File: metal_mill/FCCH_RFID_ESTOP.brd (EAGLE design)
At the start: 100 x 40 mm, 34 parts, among them Q1 2N3565, Q2 2N3565, Q3 2N3906, Q4 2N3906, Q5 2N3906

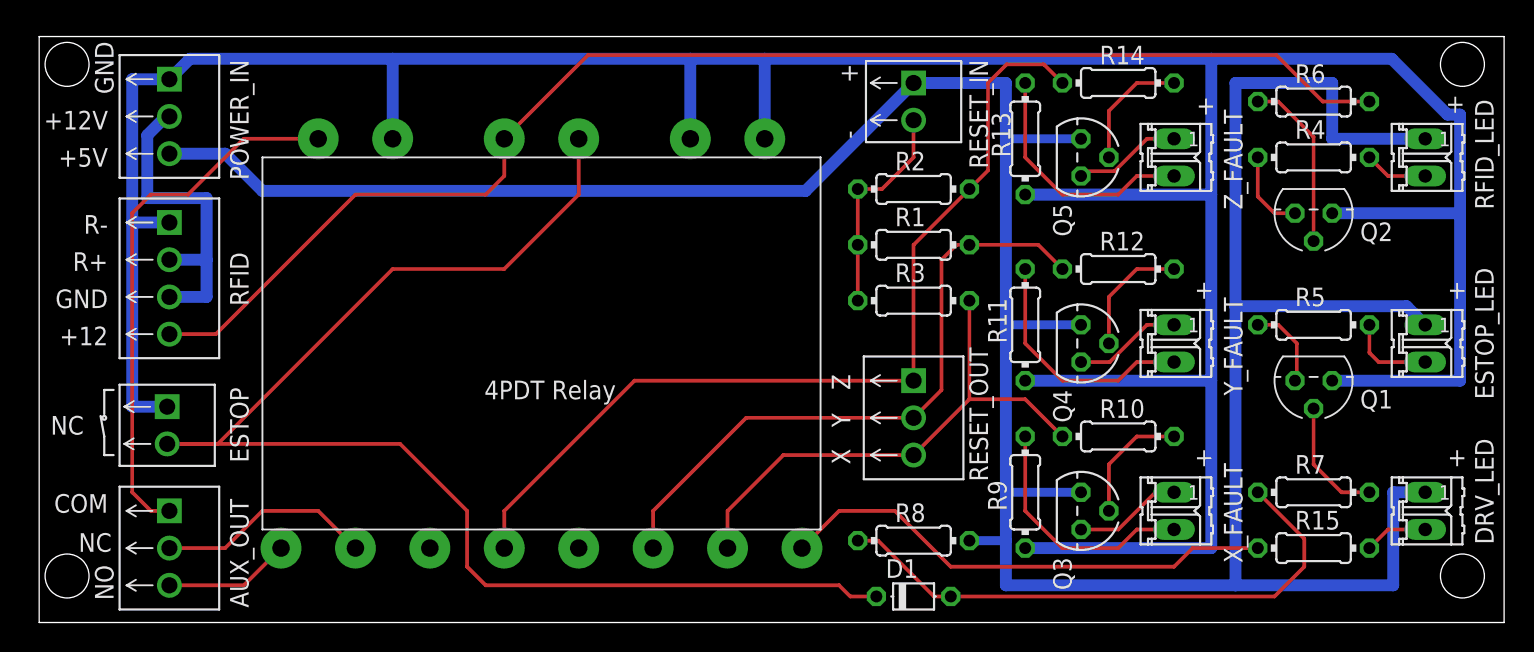
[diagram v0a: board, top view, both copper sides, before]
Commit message: check point: before changing the reset relay to allow +5V as well as ground
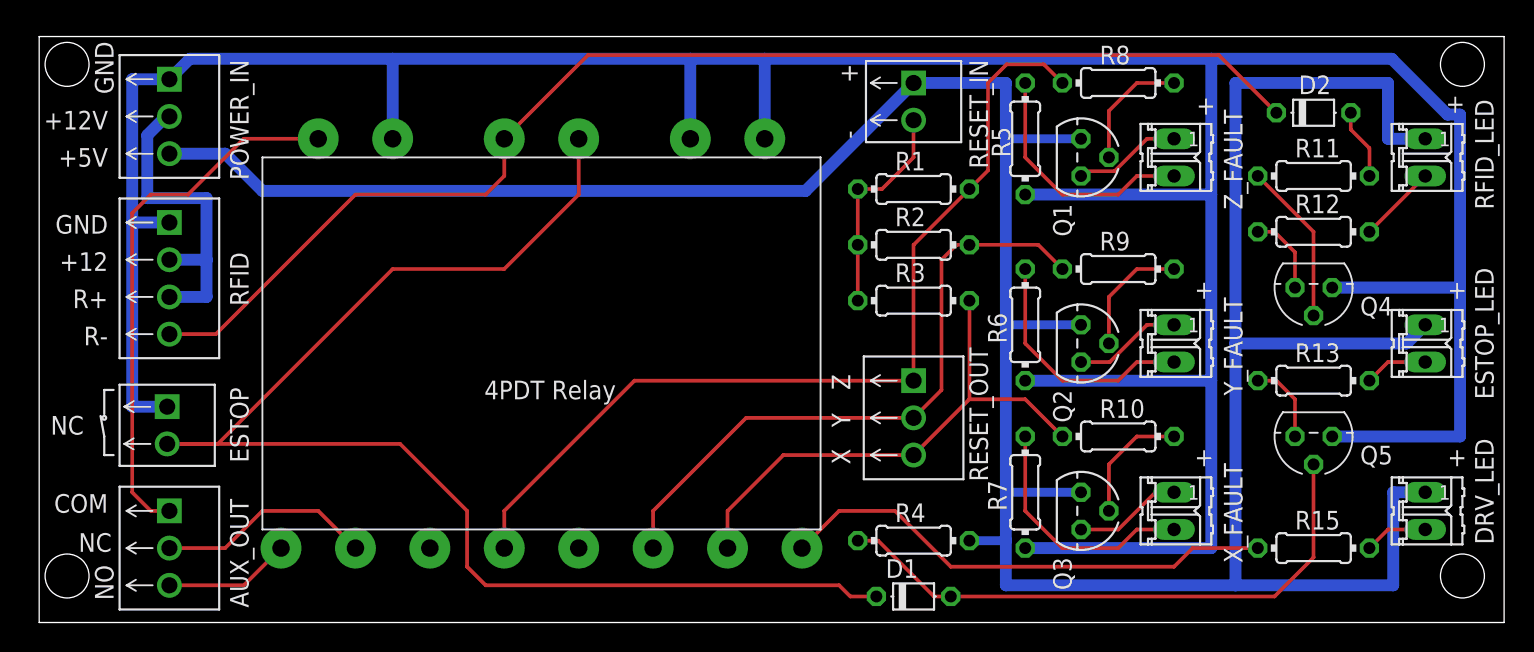
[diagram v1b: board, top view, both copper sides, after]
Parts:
- removed R14: (no value), rcl:0204/7
- added D2: (no value), diode:D-5
- Q1, Q2: value 2N3565 -> 2N3906; device transistor-npn:TO92 -> transistor-pnp:TO92
- Q4, Q5: value 2N3906 -> 2N3565; device transistor-pnp:TO92 -> transistor-npn:TO92
- R1, R2, R3: value (none) -> 4.7k
- R10, R11, R4, R8, R9: value (none) -> 2k
- R12, R13, R15, R5, R6, R7: value (none) -> 150
- moved R4 37.8 mm to (59.7, 5.59)
- moved R8 34.2 mm to (73.7, 36.8), turned to 180 degrees
- moved R13 25.7 mm to (87.0, 16.5), turned to 0 degrees
- moved R6 24.9 mm to (67.3, 20.3), turned to 90 degrees
- moved Q5 24.8 mm to (87.0, 12.7), turned to 180 degrees
- moved R5 23.4 mm to (67.3, 33.0), turned to 90 degrees
- moved R11 22.2 mm to (87.0, 30.5), turned to 0 degrees
- moved Q1 22.0 mm to (71.1, 31.8), turned to 270 degrees
- moved R7 19.7 mm to (67.3, 8.89), turned to 90 degrees
- moved Q2 18.2 mm to (71.1, 19.1), turned to 270 degrees
- moved R9 16.5 mm to (73.7, 24.1), turned to 180 degrees
- moved Q4 16.3 mm to (87.0, 22.9), turned to 180 degrees
- moved R12 13.6 mm to (87.0, 26.7), turned to 0 degrees
- moved R1 3.81 mm to (59.7, 29.6)
- moved R2 3.81 mm to (59.7, 25.8)
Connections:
- removed net N$10: Q1.2, R7.1
- new net N$1: D2.A, R11.2
- net +5V: now also Q1.3, Q2.3, R4.2; no longer Q4.3, Q5.3, R8.2
- net GND: now also Q4.3, Q5.3, R5.1, R6.1, R7.1; no longer Q1.3, Q2.3, R11.1, R13.1, R9.1
- net N$11: now also Q4.1, R12.1; no longer Q2.1, R4.1
- net N$15: now also R13.2; no longer R5.2
- net N$17: now also R12.2; no longer R4.2
- net N$20: now also Q2.2, R9.1; no longer Q4.2, R12.1
- net N$21: now also R7.2; no longer R9.2
- net N$23: now also Q2.1; no longer Q4.1
- net N$24: now also Q1.2, R8.1; no longer Q5.2, R14.1
- net N$25: now also R6.2; no longer R11.2
- net N$26: now also Q1.1; no longer Q5.1
- net N$27: now also R5.2; no longer R13.2
- net N$5: now also Q5.2, R4.1; no longer R7.2, R8.1
- net N$8: now also Q5.1, R13.1; no longer Q1.1, R5.1
- net N$9: now also Q4.2, R11.1; no longer Q2.2, R6.1
- net RFID_ENABLE: now also D2.C; no longer R6.2
- net Y_ERR/RES: now also R2.1, R9.2; no longer R1.1, R12.2
- net Z_ERR/RES: now also R1.1, R8.2; no longer R14.2, R2.1
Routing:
- net N$10: track 8.41 -> 0.00 mm
- net RFID_ENABLE: track 92.6 -> 86.6 mm
- net N$1: track 0.00 -> 4.84 mm
- net GND: track 243.6 -> 247.4 mm
- net N$15: track 5.98 -> 4.34 mm
- net N$17: track 4.34 -> 5.39 mm
- net N$5: track 39.3 -> 40.1 mm
- net N$9: track 11.9 -> 11.1 mm

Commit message: * changed reset_in to use the NO contacts of the relay * grouped the screw terminals that will connect to the GX16-8
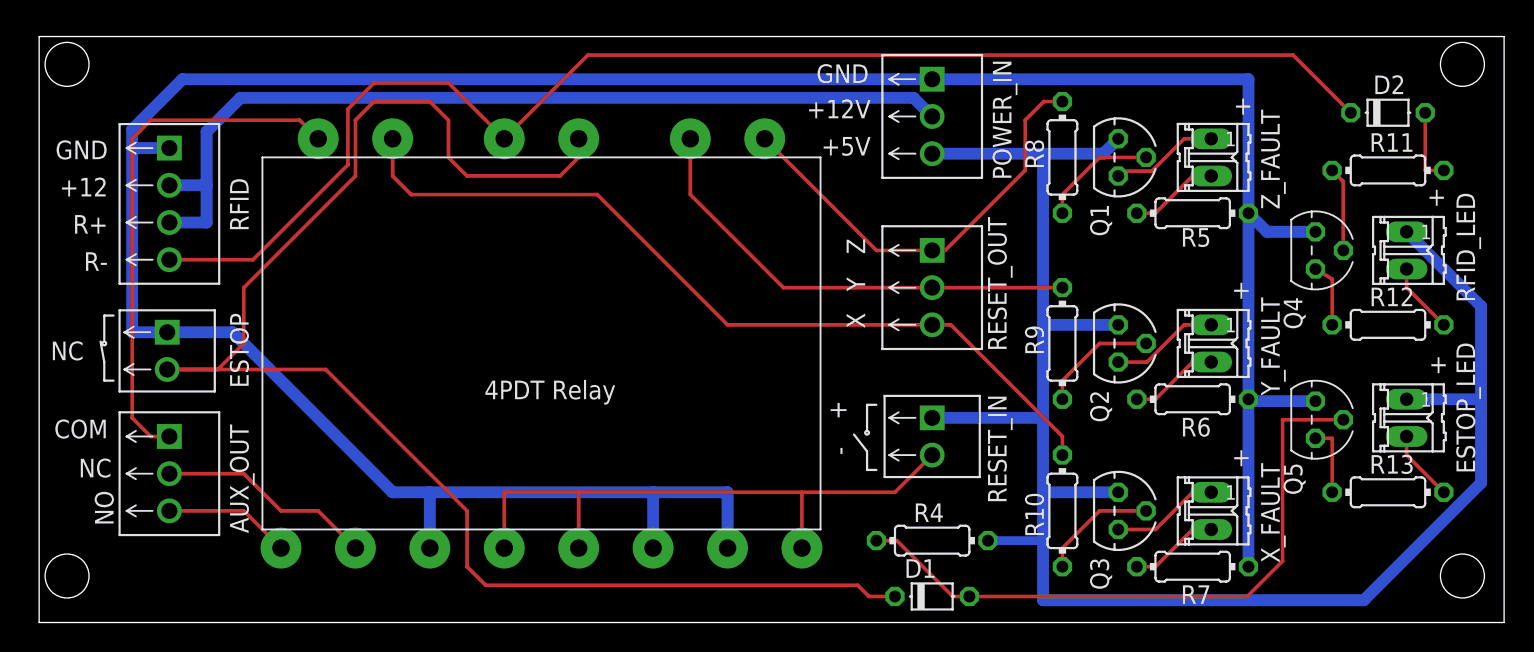
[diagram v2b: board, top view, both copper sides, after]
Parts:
- removed DRV_LED: (no value), con-amp-quick:02P
- removed R1, R2, R3: 4.7k, rcl:0204/7
- removed R15: 150, rcl:0204/7
- moved POWER_IN 52.1 mm to (61.0, 34.5)
- moved RESET_IN 22.9 mm to (61.0, 12.7)
- moved R5 12.5 mm to (78.7, 27.9), turned to 180 degrees
- moved R6 12.5 mm to (78.7, 15.2), turned to 180 degrees
- moved R7 12.5 mm to (78.7, 3.81), turned to 180 degrees
- moved R13 9.16 mm to (92.1, 8.89)
- moved RESET_OUT 8.98 mm to (61.0, 22.9)
- moved R12 8.13 mm to (92.1, 20.3)
- moved RFID_LED 6.48 mm to (93.3, 25.4)
- moved R10 6.35 mm to (69.8, 7.62), turned to 90 degrees
- moved R8 6.35 mm to (69.8, 31.8), turned to 90 degrees
- moved R9 6.35 mm to (69.8, 19.1), turned to 90 degrees
- moved ESTOP_LED 5.24 mm to (93.3, 14.0)
- moved R11 5.09 mm to (92.1, 30.9)
- moved ESTOP 5.08 mm to (8.74, 18.5)
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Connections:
- removed net ANO: R15.1, U$1.ANO
- removed net N$18: DRV_LED.2, R15.2
- removed net N$7: R1.2, R2.2, R3.2, RESET_IN.2
- new net N$2: RESET_IN.2, U$1.ANO, U$1.BNO, U$1.CNO
- net +5V: no longer DRV_LED.1
- net GND: now also U$1.ANC, U$1.BNC, U$1.CNC; no longer U$1.ACOM, U$1.BCOM, U$1.CCOM
- net X_ERR/RES: now also U$1.CCOM; no longer R3.1, U$1.ANC
- net Y_ERR/RES: now also U$1.BCOM; no longer R2.1, U$1.BNC
- net Z_ERR/RES: now also U$1.ACOM; no longer R1.1, U$1.CNO
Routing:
- net +5V: track 212.9 -> 122.7 mm
- net GND: track 247.4 -> 193.6 mm
- net N$2: track 0.00 -> 41.7 mm
- net +12V: track 22.2 -> 62.3 mm
- net ANO: track 34.3 -> 0.00 mm
- net Z_ERR/RES: track 62.7 -> 29.7 mm
- net X_ERR/RES: track 36.3 -> 56.9 mm
- net N$7: track 14.9 -> 0.00 mm
- net Y_ERR/RES: track 43.9 -> 31.8 mm
- net N$27: track 16.8 -> 6.13 mm
- net N$25: track 16.8 -> 6.13 mm
- net N$21: track 16.8 -> 6.13 mm
- net ESTOP: track 93.9 -> 103.8 mm
- net RFID_ENABLE: track 86.6 -> 93.5 mm
- net N$9: track 11.1 -> 5.78 mm
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
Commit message: fixed some mistakes found by prototyping on a breadboard. * moved wire terminals to the end of the board * updated LED devices (was using a header) * updated resistor values
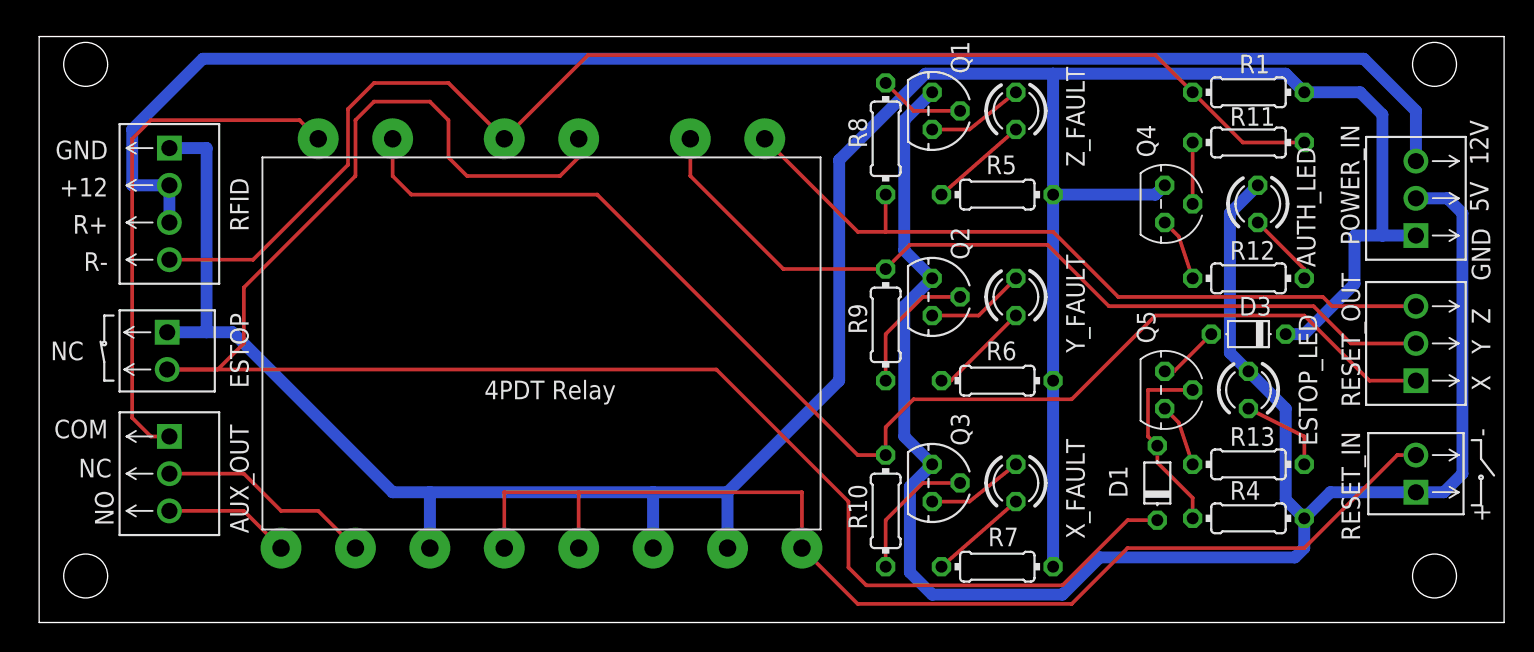
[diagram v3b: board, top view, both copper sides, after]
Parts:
- removed D2: (no value), diode:D-5
- removed RFID_LED: (no value), con-amp-quick:02P
- added AUTH_LED: SSL-LX3052GD, led:LED3MM
- added D3: 1N914, diode:D-5
- added R1: 100K, rcl:0204/7
- D1: value (none) -> 1N914
- ESTOP_LED, X_FAULT, Y_FAULT, Z_FAULT: value (none) -> SSL-LX3044LID; device con-amp-quick:02P -> led:LED3MM
- Q4, Q5: value 2N3565 -> 2N3904
- R10, R8, R9: value 2k -> 47k
- R11: value 2k -> 100K
- R12, R13: value 150 -> 82R
- R4: value 2k -> 22k
- R5, R6, R7: value 150 -> 120R
- moved POWER_IN 33.5 mm to (94.0, 29.0), turned to 180 degrees
- moved RESET_OUT 33.2 mm to (94.0, 19.1), turned to 180 degrees
- moved RESET_IN 33.1 mm to (94.0, 10.2), turned to 90 degrees
- moved R4 21.6 mm to (82.5, 7.11)
- moved D1 17.2 mm to (76.3, 9.53), turned to 90 degrees
- moved Y_FAULT 13.7 mm to (66.7, 22.2)
- moved Z_FAULT 13.7 mm to (66.7, 34.9)
- moved X_FAULT 13.5 mm to (66.7, 9.53)
- moved R5 13.4 mm to (65.4, 29.2)
- moved R6 13.4 mm to (65.4, 16.5)
- moved R7 13.3 mm to (65.4, 3.81)
- moved Q1 13.1 mm to (61.0, 34.9)
- moved Q2 13.1 mm to (61.0, 22.2)
- moved Q3 12.8 mm to (61.0, 9.53)
- moved R8 12.1 mm to (57.8, 33.0), turned to 270 degrees
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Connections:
- removed net N$19: Q3.1, X_FAULT.1
- removed net N$21: R7.2, X_FAULT.2
- removed net N$23: Q2.1, Y_FAULT.1
- removed net N$25: R6.2, Y_FAULT.2
- removed net N$26: Q1.1, Z_FAULT.1
- removed net N$27: R5.2, Z_FAULT.2
- new net N$10: Q2.1, Y_FAULT.A
- new net N$11: R5.2, Z_FAULT.K
- new net N$12: Q1.1, Z_FAULT.A
- new net N$7: D3.A, Q5.3
- new net N$8: Q3.1, X_FAULT.A
- new net N$9: R6.2, Y_FAULT.K
- net +12V: now also POWER_IN.3; no longer POWER_IN.2
- net +5V: now also AUTH_LED.A, ESTOP_LED.A, POWER_IN.2; no longer ESTOP_LED.1, POWER_IN.3, RFID_LED.1
- net GND: now also D3.C, R1.2; no longer Q5.3
- net N$1: now also R7.2, X_FAULT.K; no longer D2.A, R11.2
- net N$15: now also ESTOP_LED.K; no longer ESTOP_LED.2
- net N$17: now also AUTH_LED.K; no longer RFID_LED.2
- net RFID_ENABLE: now also R1.1, R11.2; no longer D2.C
- net X_ERR/RES: now also RESET_OUT.1; no longer RESET_OUT.3
- net Z_ERR/RES: now also RESET_OUT.3; no longer RESET_OUT.1
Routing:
- net +12V: track 62.3 -> 103.4 mm
- net N$2: track 41.7 -> 79.4 mm
- net N$5: track 44.1 -> 13.1 mm
- net X_ERR/RES: track 56.9 -> 87.2 mm
- net Y_ERR/RES: track 31.8 -> 58.2 mm
- net Z_ERR/RES: track 29.7 -> 51.7 mm
- net ESTOP: track 103.8 -> 123.7 mm
- net N$19: track 7.40 -> 0.00 mm
- net N$23: track 7.40 -> 0.00 mm
- net N$26: track 7.40 -> 0.00 mm
- net N$9: track 0.00 -> 6.92 mm
- net N$10: track 0.00 -> 6.77 mm
- net N$11: track 0.00 -> 6.75 mm
- net N$8: track 0.00 -> 6.61 mm
- net N$12: track 0.00 -> 6.61 mm
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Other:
- board text added: "12V"
- board text added: "5V"
- board text removed: "+12V"
- board text removed: "+5V"
